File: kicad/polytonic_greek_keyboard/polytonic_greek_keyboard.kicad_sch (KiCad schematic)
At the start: 5 parts, among them J1 USB_C_Receptacle, J4 Conn_01x11_Socket, J5 Conn_01x11_Pin, U4 MCP23017_SP, U5 MCP23017_SP

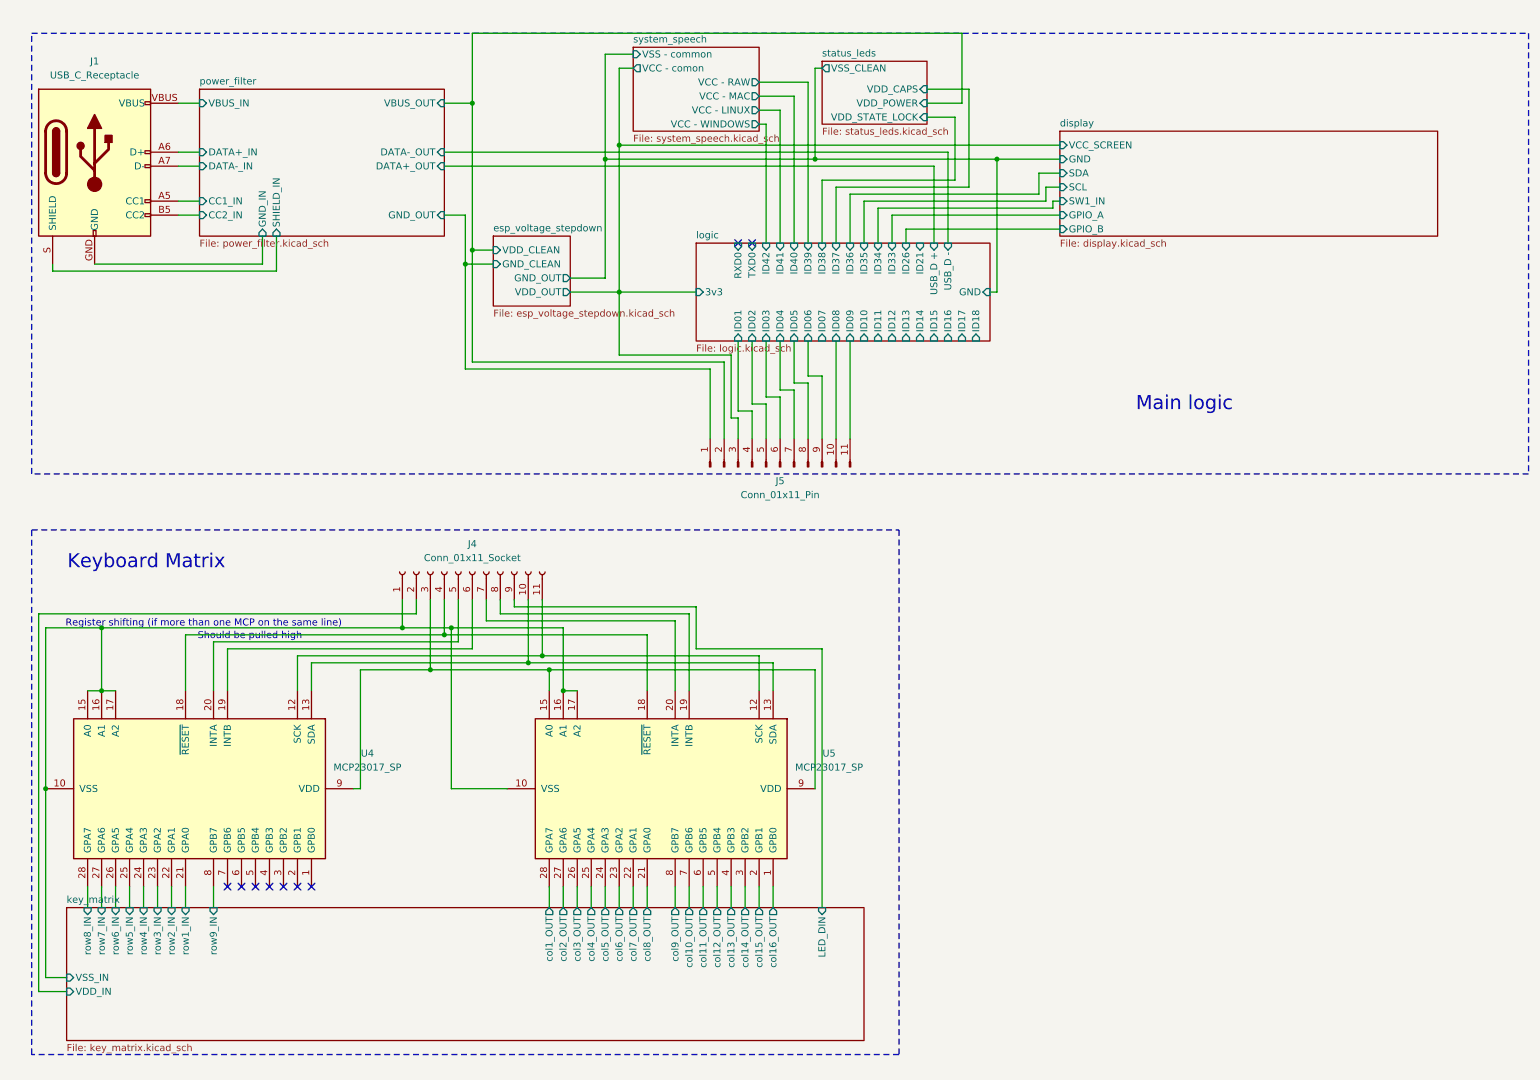
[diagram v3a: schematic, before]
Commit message: [UPDATE] the desing to fit on two separate pcbs
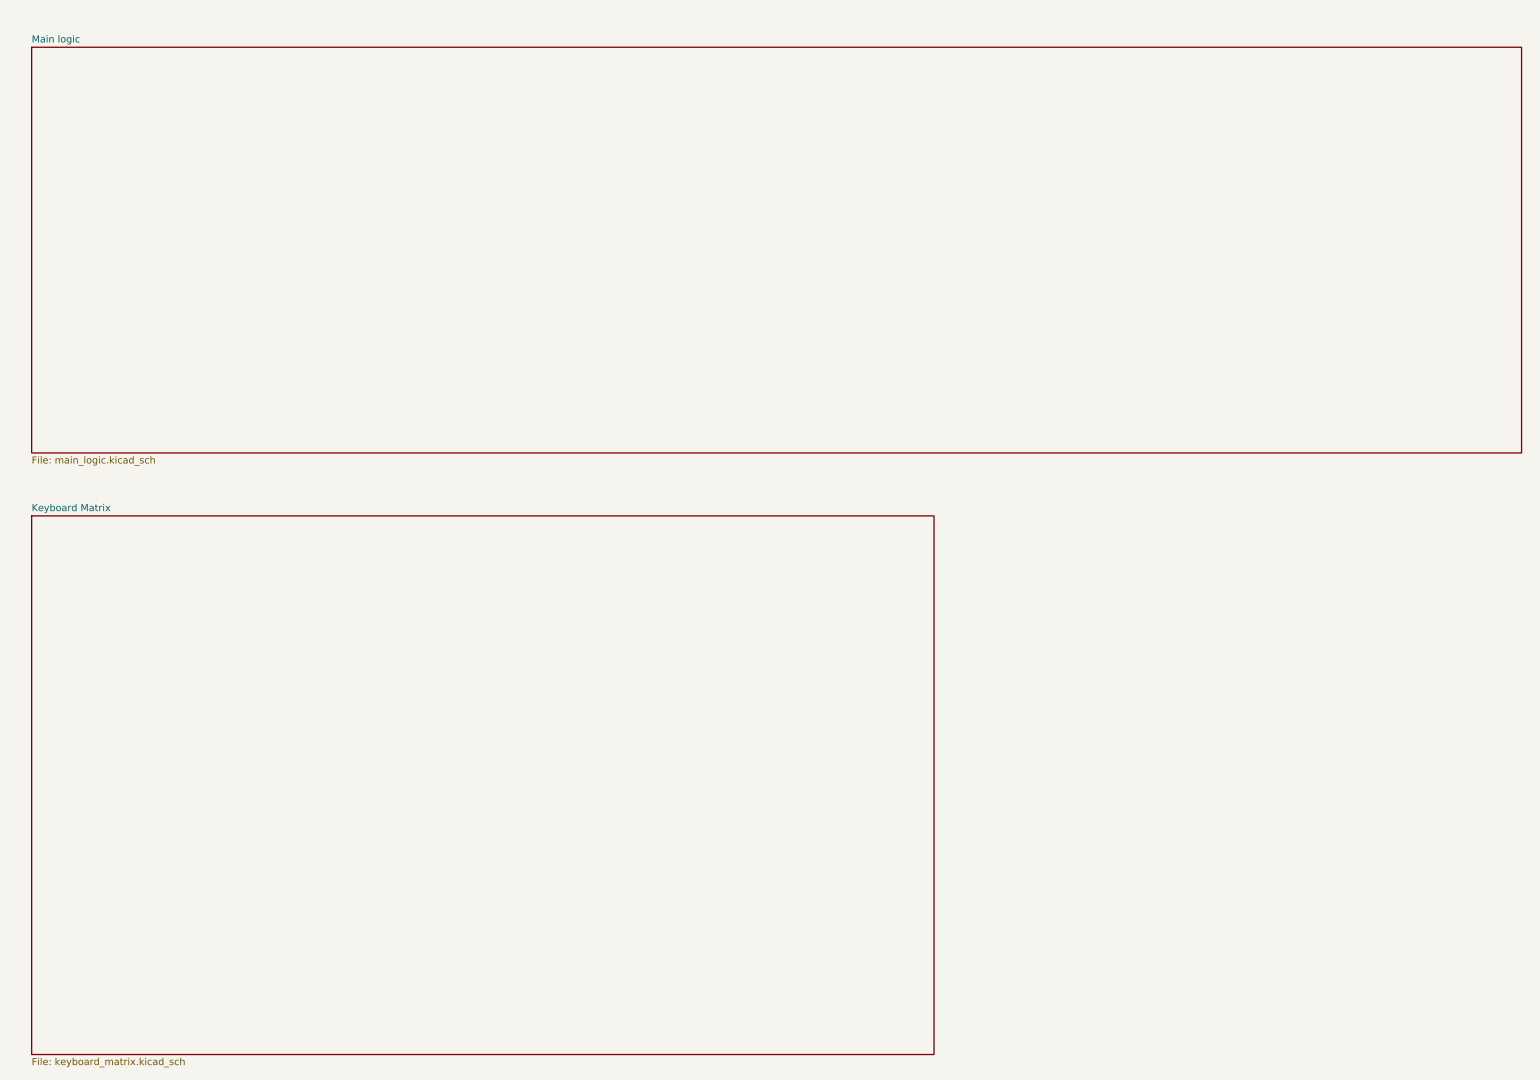
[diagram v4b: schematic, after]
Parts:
- removed J1: USB_C_Receptacle, PCM_SparkFun-Connector:USB-C_16, symbol PCM_SparkFun-Connector:USB_C_Receptacle
- removed J4: Conn_01x11_Socket, Connector_PinSocket_2.00mm:PinSocket_1x11_P2.00mm_Horizontal, symbol Connector:Conn_01x11_Socket
- removed J5: Conn_01x11_Pin, Connector_PinHeader_2.00mm:PinHeader_1x11_P2.00mm_Horizontal, symbol Connector:Conn_01x11_Pin
- removed U4, U5: MCP23017_SP, Package_DIP:DIP-28_W7.62mm, symbol Interface_Expansion:MCP23017_SP
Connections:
- no-connect marks 9 -> 0
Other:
- removed sheet display
- removed sheet esp_voltage_stepdown
- removed sheet key_matrix
- removed sheet logic
- removed sheet power_filter
- removed sheet status_leds
- removed sheet system_speech
- added sheet Keyboard Matrix (keyboard_matrix.kicad_sch)
- added sheet Main logic (main_logic.kicad_sch)
- note removed: "Keyboard Matrix"
- note removed: "Main logic"
- note removed: "Register shifting (if more than one MCP on the same line)"
- note removed: "Should be pulled high"

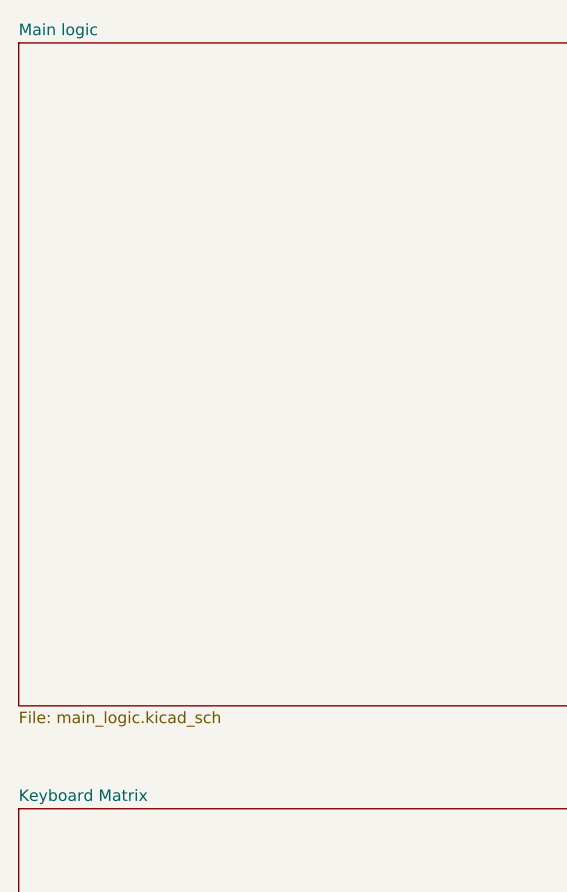
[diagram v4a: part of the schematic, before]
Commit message: [UPDATE] file name keyboard_main_logic.kicad_pcb to driver.kicad_pcb
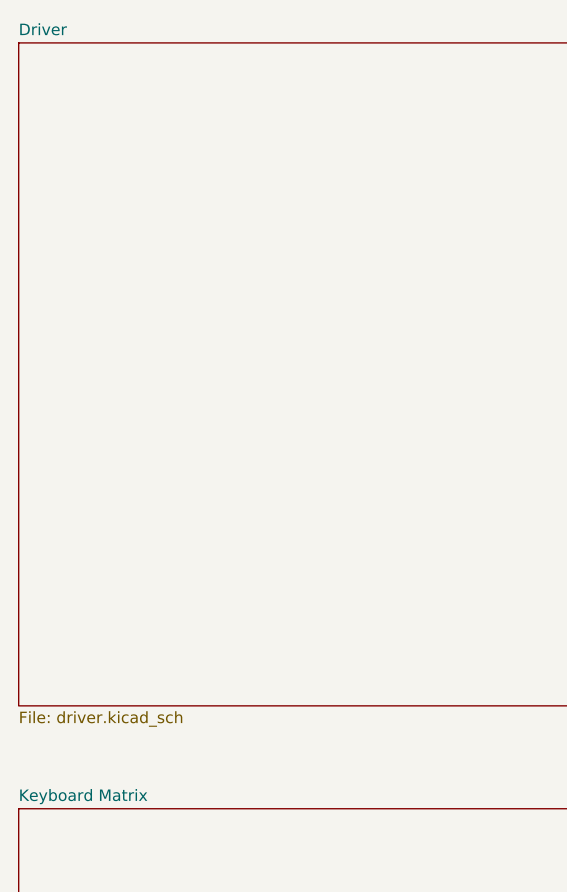
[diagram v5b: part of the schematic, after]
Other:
- sheet Main logic renamed Driver
- sheet Driver: file main_logic.kicad_sch -> driver.kicad_sch
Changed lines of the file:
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@@
 			(color 255 168 118 1.0000)
 		)
-		(property "Sheetname" "Main logic"
+		(property "Sheetname" "Driver"
 			(at 12.7 14.5284 0)
 			(effects
@@
 			)
 		)
-		(property "Sheetfile" "main_logic.kicad_sch"
+		(property "Sheetfile" "driver.kicad_sch"
 			(at 12.7 89.4846 0)
 			(effects
@@
 		)
 		(instances
-			(project "polytonic_greek_keyboard"
+			(project "keyboard_driver"
 				(path "/cbe25a1b-6c02-43c2-9ff9-ba274c7cf6a2"
 					(page "21")
@@
 		)
 		(instances
-			(project "polytonic_greek_keyboard"
+			(project "keyboard_driver"
 				(path "/cbe25a1b-6c02-43c2-9ff9-ba274c7cf6a2"
 					(page "22")

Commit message: [UPDATE] the final merged version of the schematic before splitting into two separate kicad projects
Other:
- company: (none) -> Henry's Software House
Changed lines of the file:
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@@
 		(title "Main level")
 		(date "2025-10-01")
+		(rev "1 - do not edit connector pin layout.")
+		(company "Henry's Software House")
 		(comment 1 "This is where the main logic of the sheet is located.")
 		(comment 2 "This provides a high level overview without ")
